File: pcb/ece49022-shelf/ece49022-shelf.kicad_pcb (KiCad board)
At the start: 2 copper layers, 65 parts, among them IC1 NAU7802, J1 USB_B_Micro, J2 Conn_01x16_Pin, J3 Conn_01x04_Pin, J4 SM03B-SRSS-TB, J6 Conn_01x02_Pin, J7 Conn_01x02_Pin, SW1 SW_Push, SW2 SW_Push, U2 TPS54202DDCT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

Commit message: Started Layout
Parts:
- removed R12: 0, Resistor_SMD:R_0402_1005Metric
- added C32: 0.1uF, 25V, Capacitor_SMD:C_0402_1005Metric, F.Cu at (203.2, 52.1)
- added C6: 0.1uF, 25V, Capacitor_SMD:C_0402_1005Metric, F.Cu at (202.7, 50.4)
- moved R4 59.0 mm to (207.3, 53.9), turned to 90 degrees
- moved R3 57.6 mm to (205.9, 52.7), turned to 90 degrees
- moved IC1 56.9 mm to (197.8, 55.3)
- moved C4 56.5 mm to (191.6, 50.3), turned to 90 degrees
- moved J7 56.1 mm to (173.6, 121.2), turned to 90 degrees
- moved C3 55.1 mm to (192.9, 50.3), turned to 90 degrees
- moved J6 54.8 mm to (96.7, 37.7)
- moved C5 51.9 mm to (192.9, 57.7), turned to 90 degrees
- moved C2 51.0 mm to (192.9, 52.8), turned to -90 degrees
- moved R2 48.2 mm to (189.7, 53.5)
- moved R1 47.4 mm to (189.7, 52.3)
- moved C1 47.0 mm to (192.9, 55.3), turned to -90 degrees
- moved H1 41.9 mm to (129.3, 43.1)
- moved J3 40.7 mm to (92.1, 52.1)
- moved R15 40.5 mm to (175.6, 99.6), turned to -90 degrees
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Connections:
- R13 pad 2: /RP2350A/FLASH_SS -> /RP2350A/QSPI_SS
- U3 pad 1: /RP2350A/FLASH_SS -> /RP2350A/QSPI_SS
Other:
- board outline added: 80 x 60 mm
- board text added: "NEED TO FIX VCC LABEL"

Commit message: stuff
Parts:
- C1, C3, C4: footprint 49022_Footprints:C_0402_1005Metric_small_pads -> Capacitor_SMD:C_0402_1005Metric_Pad0.74x0.62mm_HandSolder
- C32, C5: footprint Capacitor_SMD:C_0402_1005Metric -> Capacitor_SMD:C_0402_1005Metric_Pad0.74x0.62mm_HandSolder
- R11: footprint Resistor_SMD:R_0402_1005Metric -> Resistor_SMD:R_0805_2012Metric_Pad1.20x1.40mm_HandSolder
- moved J2 94.8 mm to (187.2, 68.8), turned to -90 degrees
- moved J6 89.6 mm to (149.7, 110.0), turned to 90 degrees
- moved R13 63.2 mm to (184.9, 80.2)
- moved R17 63.2 mm to (186.0, 80.2)
- moved J1 57.8 mm to (177.0, 121.2), turned to 0 degrees
- moved SW1 56.1 mm to (181.4, 79.3)
- moved U3 55.8 mm to (184.4, 86.0), turned to -90 degrees
- moved J4 54.6 mm to (197.0, 105.0)
- moved J3 54.5 mm to (143.9, 69.0), turned to -90 degrees
- moved C30 49.8 mm to (183.9, 91.7), turned to 0 degrees
- moved C29 48.8 mm to (183.9, 92.8), turned to 0 degrees
- moved R4 48.2 mm to (171.0, 85.6), turned to -90 degrees
- moved C16 48.0 mm to (179.8, 89.2), turned to 90 degrees
- moved R18 47.9 mm to (183.9, 93.9), turned to 180 degrees
- moved R3 47.1 mm to (172.2, 85.6), turned to -90 degrees
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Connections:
- C32 pad 1: VCC -> +5V
- IC1 pad 15: VCC -> +5V
- R3 pad 2: VCC -> +5V
- R4 pad 2: VCC -> +5V
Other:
- copper layers 2 -> 4

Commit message: stuff
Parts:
- added C18: 4.7u, Capacitor_SMD:C_0402_1005Metric_Pad0.74x0.62mm_HandSolder, F.Cu at (10.1, 0.48)
- added C19: 4.7u, Capacitor_SMD:C_0402_1005Metric_Pad0.74x0.62mm_HandSolder, F.Cu at (10.1, 2.46)
- added C2: 0.1uF, 16V, Capacitor_SMD:C_0402_1005Metric_Pad0.74x0.62mm_HandSolder, F.Cu at (10.1, 14.3)
- added C20: 100n, Capacitor_SMD:C_0402_1005Metric_Pad0.74x0.62mm_HandSolder, F.Cu at (10.1, 4.42)
- added C21: 4.7u, Capacitor_SMD:C_0402_1005Metric_Pad0.74x0.62mm_HandSolder, F.Cu at (10.1, 6.39)
- added C23: 100n, Capacitor_SMD:C_0402_1005Metric_Pad0.74x0.62mm_HandSolder, F.Cu at (10.1, 8.37)
- added C25: 100n, Capacitor_SMD:C_0402_1005Metric_Pad0.74x0.62mm_HandSolder, F.Cu at (10.1, 10.3)
- added C26: 100n, Capacitor_SMD:C_0402_1005Metric_Pad0.74x0.62mm_HandSolder, F.Cu at (13.3, 0.48)
- added C27: 100n, Capacitor_SMD:C_0402_1005Metric_Pad0.74x0.62mm_HandSolder, F.Cu at (13.3, 2.46)
- added C28: 100n, Capacitor_SMD:C_0402_1005Metric_Pad0.74x0.62mm_HandSolder, F.Cu at (13.3, 4.42)
- added C29: 100n, Capacitor_SMD:C_0402_1005Metric_Pad0.74x0.62mm_HandSolder, F.Cu at (13.3, 6.39)
- added C3: 0.1uF, 50V, Capacitor_SMD:C_0402_1005Metric_Pad0.74x0.62mm_HandSolder, F.Cu at (10.1, 16.3)
- added C30: 100n, Capacitor_SMD:C_0402_1005Metric_Pad0.74x0.62mm_HandSolder, F.Cu at (13.3, 8.37)
- added C32: 0.1uF, 50V, Capacitor_SMD:C_0402_1005Metric_Pad0.74x0.62mm_HandSolder, F.Cu at (10.1, 20.2)
- added C6: 0.1uF, 50V, Capacitor_SMD:C_0402_1005Metric_Pad0.74x0.62mm_HandSolder, F.Cu at (10.1, 18.2)
- added H1: MountingHole, MountingHole:MountingHole_2.7mm_M2.5, F.Cu at (2.98, 2.98)
- added H2: MountingHole, MountingHole:MountingHole_2.7mm_M2.5, F.Cu at (2.98, 9.93)
- added H3: MountingHole, MountingHole:MountingHole_2.7mm_M2.5, F.Cu at (2.98, 16.9)
- added H4: MountingHole, MountingHole:MountingHole_2.7mm_M2.5, F.Cu at (2.98, 23.8)
- added R1: 47, 1%, Resistor_SMD:R_0402_1005Metric_Pad0.72x0.64mm_HandSolder, F.Cu at (13.3, 14.3)
- added R2: 47, 1%, Resistor_SMD:R_0402_1005Metric_Pad0.72x0.64mm_HandSolder, F.Cu at (13.3, 16.3)
- C18, C19, C20, C21, C22, C23, C24, C25, C26, C27, C28, C29, C30: footprint Capacitor_SMD:C_0402_1005Metric -> Capacitor_SMD:C_0402_1005Metric_Pad0.74x0.62mm_HandSolder
- C2: value 0.1uF, 25V -> 0.1uF, 16V; footprint Capacitor_SMD:C_0402_1005Metric -> Capacitor_SMD:C_0402_1005Metric_Pad0.74x0.62mm_HandSolder
- C3, C32, C5: value 0.1uF, 25V -> 0.1uF, 50V
- C6: value 0.1uF, 25V -> 0.1uF, 50V; footprint Capacitor_SMD:C_0402_1005Metric -> Capacitor_SMD:C_0402_1005Metric_Pad0.74x0.62mm_HandSolder
- R1, R2: value 47, 0.1% -> 47, 1%
- R16: footprint Resistor_SMD:R_0402_1005Metric -> Resistor_SMD:R_0402_1005Metric_Pad0.72x0.64mm_HandSolder
- moved H1 78.6 mm to (202.0, 73.0)
- moved J3 54.7 mm to (171.4, 116.3), turned to 90 degrees
- moved R8 44.0 mm to (171.6, 100.2), turned to -90 degrees
- moved C12 43.1 mm to (172.6, 102.3), turned to -90 degrees
- moved R9 42.1 mm to (171.6, 102.2), turned to -90 degrees
- moved C11 41.4 mm to (170.0, 101.2), turned to -90 degrees
- moved C10 39.4 mm to (167.9, 101.2), turned to -90 degrees
- moved R2 38.7 mm to (178.9, 111.6), turned to -90 degrees
- moved R1 38.4 mm to (177.7, 111.6), turned to -90 degrees
- moved C5 38.3 mm to (183.4, 110.0), turned to 180 degrees
- moved R10 37.2 mm to (172.0, 108.1), turned to 90 degrees
- moved C9 36.7 mm to (169.2, 105.0), turned to 0 degrees
- moved C1 36.6 mm to (180.9, 110.0), turned to 0 degrees
- moved C3 35.8 mm to (176.5, 110.4), turned to -90 degrees
- moved J6 35.3 mm to (184.4, 116.3)
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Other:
- board size 80 x 60 mm -> 59.2 x 49.6 mm

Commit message: Initial Placement done
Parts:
- removed the C18 at (10.1, 0.48)
- removed the C19 at (10.1, 2.46)
- removed the C2 at (10.1, 14.3)
- removed the C20 at (10.1, 4.42)
- removed the C21 at (10.1, 6.39)
- removed the C23 at (10.1, 8.37)
- removed the C25 at (10.1, 10.3)
- removed the C26 at (13.3, 0.48)
- removed the C27 at (13.3, 2.46)
- removed the C28 at (13.3, 4.42)
- removed the C29 at (13.3, 6.39)
- removed the C3 at (10.1, 16.3)
- removed the C30 at (13.3, 8.37)
- removed the C32 at (10.1, 20.2)
- removed the C6 at (10.1, 18.2)
- removed the H1 at (2.98, 2.98)
- removed the R1 at (13.3, 14.3)
- removed the R2 at (13.3, 16.3)
- moved H4 210.0 mm to (194.0, 111.0)
- moved H2 200.6 mm to (194.0, 71.0)
- moved H3 164.2 mm to (158.0, 71.0)
- moved H1 58.1 mm to (158.0, 111.0)
- moved U3 10.7 mm to (185.0, 72.0)
- moved J1 8.90 mm to (195.2, 85.4)
- moved J2 8.20 mm to (195.1, 65.0)
- moved R11 7.74 mm to (164.4, 70.0), turned to -90 degrees
- moved J4 7.31 mm to (194.1, 95.0)
- moved SW1 7.26 mm to (186.2, 80.0), turned to 90 degrees
- moved C1 6.16 mm to (182.8, 104.1)
- moved IC1 6.16 mm to (182.8, 99.1)
- moved R2 6.16 mm to (180.8, 105.7)
- moved R3 6.16 mm to (180.8, 93.5)
- moved C2 6.16 mm to (180.2, 103.9)
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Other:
- board size 59.2 x 49.6 mm -> 44.2 x 53.6 mm
- board text removed: "NEED TO FIX VCC LABEL"

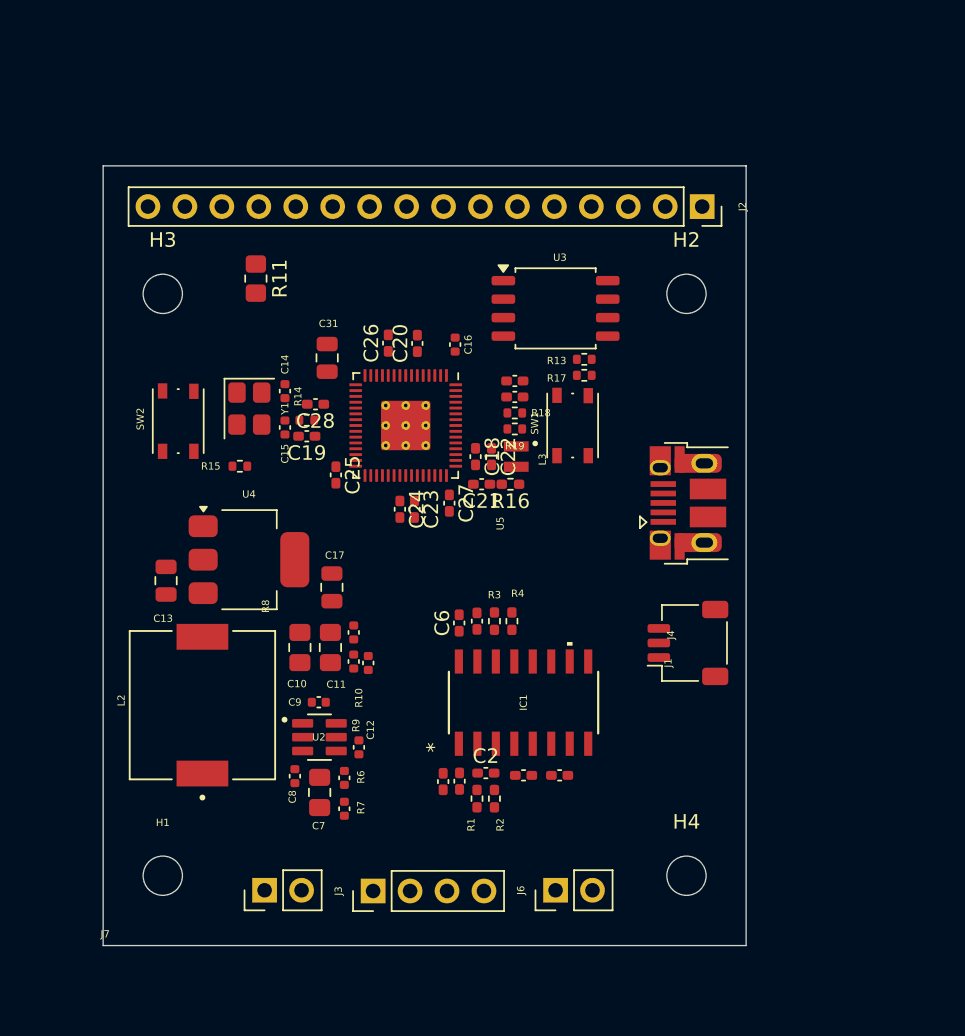
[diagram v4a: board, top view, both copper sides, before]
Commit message: cap footprints for MCU smps needed to change
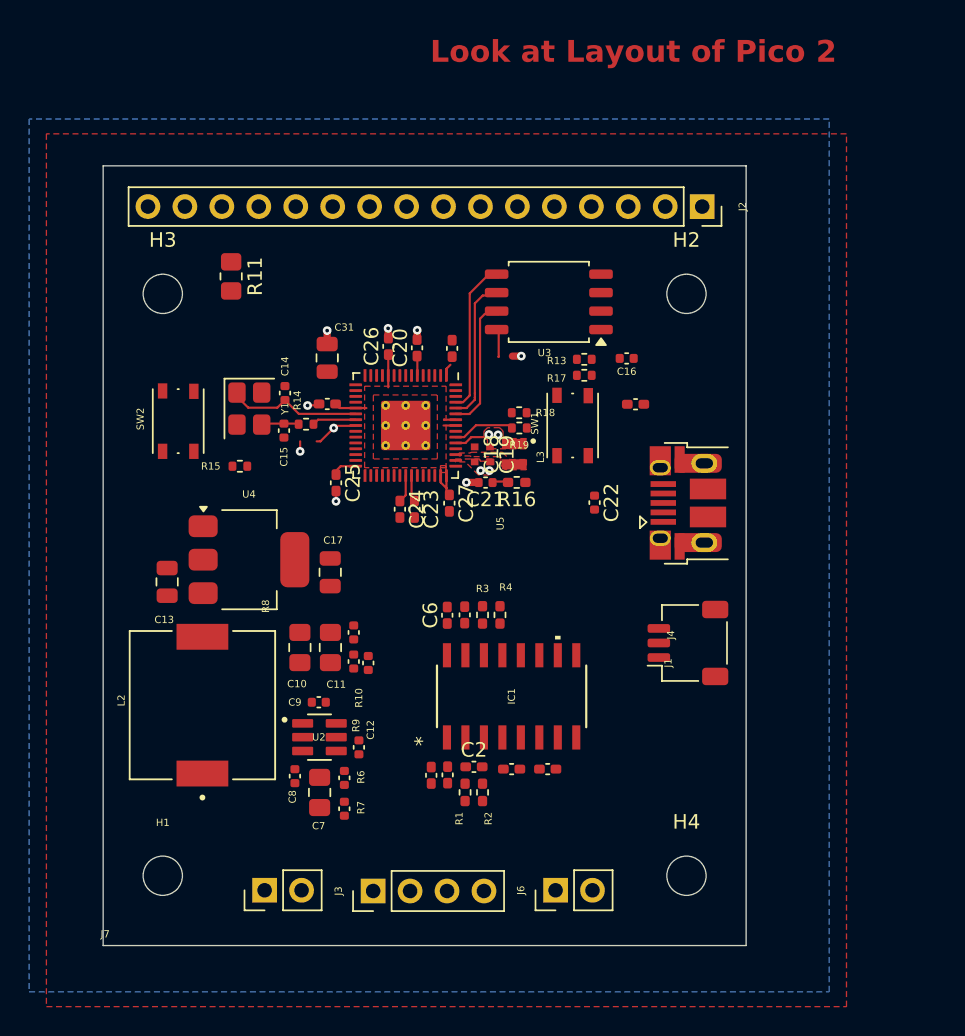
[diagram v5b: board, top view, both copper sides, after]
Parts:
- C18, C19: footprint Capacitor_SMD:C_0402_1005Metric_Pad0.74x0.62mm_HandSolder -> 49022_Footprints:C_0402_1005Metric_small_pads
- C21, C22: footprint Capacitor_SMD:C_0402_1005Metric_Pad0.74x0.62mm_HandSolder -> Capacitor_SMD:C_0402_1005Metric
- moved C19 12.7 mm to (180.5, 82.0), turned to -90 degrees
- moved C16 11.8 mm to (189.9, 75.4), turned to 0 degrees
- moved C29 8.32 mm to (190.5, 78.6)
- moved C22 7.75 mm to (187.7, 85.3)
- moved C30 4.86 mm to (177.9, 74.8), turned to 90 degrees
- moved R11 1.71 mm to (162.7, 69.8)
- moved C17 1.04 mm to (169.5, 90.1)
- moved C6 0.98 mm to (177.6, 93.1)
- moved C32 0.95 mm to (178.8, 93.1)
- moved R2 0.93 mm to (180.0, 105.3)
- moved R3 0.93 mm to (180.0, 93.1)
- moved C1 0.93 mm to (182.0, 103.7)
- moved C2 0.93 mm to (179.4, 103.5)
- moved IC1 0.93 mm to (182.0, 98.7)
- moved C3 0.93 mm to (177.6, 104.1)
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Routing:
- net +3V3: track 0.00 -> 14.8 mm
- net /RP2350A/QSPI_SD0: track 0.00 -> 10.6 mm
- net /RP2350A/QSPI_SCLK: track 0.00 -> 10.0 mm
- net /RP2350A/XIN: track 0.00 -> 9.36 mm
- net /RP2350A/QSPI_SD3: track 0.00 -> 9.22 mm
- net +1V1: track 0.00 -> 8.97 mm, vias 0 -> 3
- net GND: track 0.00 -> 5.89 mm, vias 0 -> 10
- net Net-(U5-USB_DM): track 0.00 -> 3.96 mm
- net /RP2350A/XOUT: track 0.00 -> 3.11 mm
- net Net-(C15-Pad1): track 0.00 -> 2.65 mm
- net /RP2350A/VREG_AVDD: track 0.00 -> 1.11 mm
- added copper zone on F.Cu, net +1V1
- added copper zone on B.Cu, net +3V3
- added copper zone on F.Cu, net +3V3
- added copper zone on F.Cu, net /RP2350A/VREG_LX
- added copper zone on F.Cu, net GND
- added copper zone on In1.Cu, net GND
- added copper zone on In2.Cu, net GND
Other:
- board text added: "Look at Layout of Pico 2"

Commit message: stuff
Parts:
- C21, C22: footprint Capacitor_SMD:C_0402_1005Metric -> Capacitor_SMD:C_0402_1005Metric_Pad0.74x0.62mm_HandSolder
- R14: footprint Resistor_SMD:R_0402_1005Metric -> Resistor_SMD:R_0402_1005Metric_Pad0.72x0.64mm_HandSolder
- moved C22 20.2 mm to (168.0, 81.0), turned to 180 degrees
- moved SW1 8.02 mm to (184.6, 87.9)
- moved R13 6.39 mm to (188.1, 81.8)
- moved R17 6.39 mm to (188.1, 82.9)
- moved C16 5.58 mm to (188.1, 80.7)
- moved C29 5.58 mm to (188.7, 83.9)
- moved R18 1.92 mm to (184.4, 79.3)
- moved R19 1.90 mm to (184.4, 80.4)
- moved U3 1.56 mm to (183.1, 72.1), turned to -90 degrees
- moved C21 0.52 mm to (180.1, 84.5)
- moved R16 0.50 mm to (182.4, 84.5)
- moved R14 0.15 mm to (168.0, 80.0)
- moved L3 0.11 mm to (182.3, 82.0)
- moved C18 0.10 mm to (179.5, 82.0)
- moved C19 0.10 mm to (180.6, 82.0)
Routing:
- net Net-(U5-USB_DP): track 0.00 -> 6.22 mm
- net /RP2350A/QSPI_SD0: track 10.6 -> 4.79 mm
- net /RP2350A/VREG_AVDD: track 1.11 -> 5.46 mm
- net /RP2350A/QSPI_SCLK: track 10.0 -> 6.04 mm
- net Net-(U5-USB_DM): track 3.96 -> 6.20 mm
- net /RP2350A/QSPI_SS: track 0.00 -> 1.94 mm, vias 0 -> 1
- net /RP2350A/QSPI_SD3: track 9.22 -> 7.34 mm
- net GND: track 5.89 -> 7.66 mm, vias 10 -> 11
- net +3V3: track 14.8 -> 13.1 mm
- net /RP2350A/QSPI_SD1: track 0.00 -> 1.08 mm, vias 0 -> 1

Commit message: routing
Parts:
- C9: moved to B.Cu
- moved J4 38.1 mm to (157.7, 83.7), turned to -90 degrees
- moved SW2 20.4 mm to (140.4, 88.1), turned to 180 degrees
- moved R15 16.8 mm to (146.7, 80.3)
- moved R13 12.7 mm to (185.8, 69.3), turned to 135 degrees
- moved R17 11.7 mm to (188.8, 71.2)
- moved C29 10.8 mm to (178.9, 79.3)
- moved C16 5.39 mm to (189.4, 75.5), turned to -45 degrees
- moved J1 4.10 mm to (195.2, 81.3)
- moved C9 3.33 mm to (168.7, 102.4), turned to 45 degrees
- moved C3 2.88 mm to (176.9, 106.9)
- moved C4 2.88 mm to (175.8, 106.9)
- moved R1 2.88 mm to (178.1, 108.1)
- moved C32 2.88 mm to (178.1, 95.9)
- moved R2 2.88 mm to (179.3, 108.1)
- moved C6 2.88 mm to (176.9, 95.9)
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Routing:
- net /LCD_RS/DI: track 0.00 -> 21.7 mm
- net /LCD_R_W: track 0.00 -> 19.9 mm
- net /LCD_E: track 0.00 -> 17.8 mm
- net /LCD_DB7: track 0.00 -> 17.7 mm
- net GND: track 7.66 -> 24.0 mm, vias 11 -> 36
- net /LCD_DB0: track 0.00 -> 15.8 mm
- net /LCD_DB6: track 0.00 -> 15.8 mm
- net /RP2350A/QSPI_SS: track 1.94 -> 16.9 mm, vias 1 -> 0
- net /LCD_DB5: track 0.00 -> 14.0 mm
- net /LCD_DB1: track 0.00 -> 13.7 mm
- net /LCD_DB2: track 0.00 -> 12.9 mm
- net /LCD_DB4: track 0.00 -> 12.8 mm
- net /LCD_DB3: track 0.00 -> 12.0 mm
- net /RP2350A/QSPI_SD2: track 0.00 -> 11.9 mm
- net /RP2350A/QSPI_SD1: track 1.08 -> 13.0 mm, vias 1 -> 0
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- added copper zone on F.Cu, net +5V
- added copper zone on F.Cu, net AVDD
- added copper zone on B.Cu, net Net-(U2-BOOT)
- added copper zone on F.Cu, net Net-(U2-BOOT)
- added copper zone on B.Cu, net Net-(U2-SW)
- added copper zone on F.Cu, net Net-(U2-SW)
